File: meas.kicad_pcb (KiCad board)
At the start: 2 copper layers, 100 x 220 mm, 3 parts

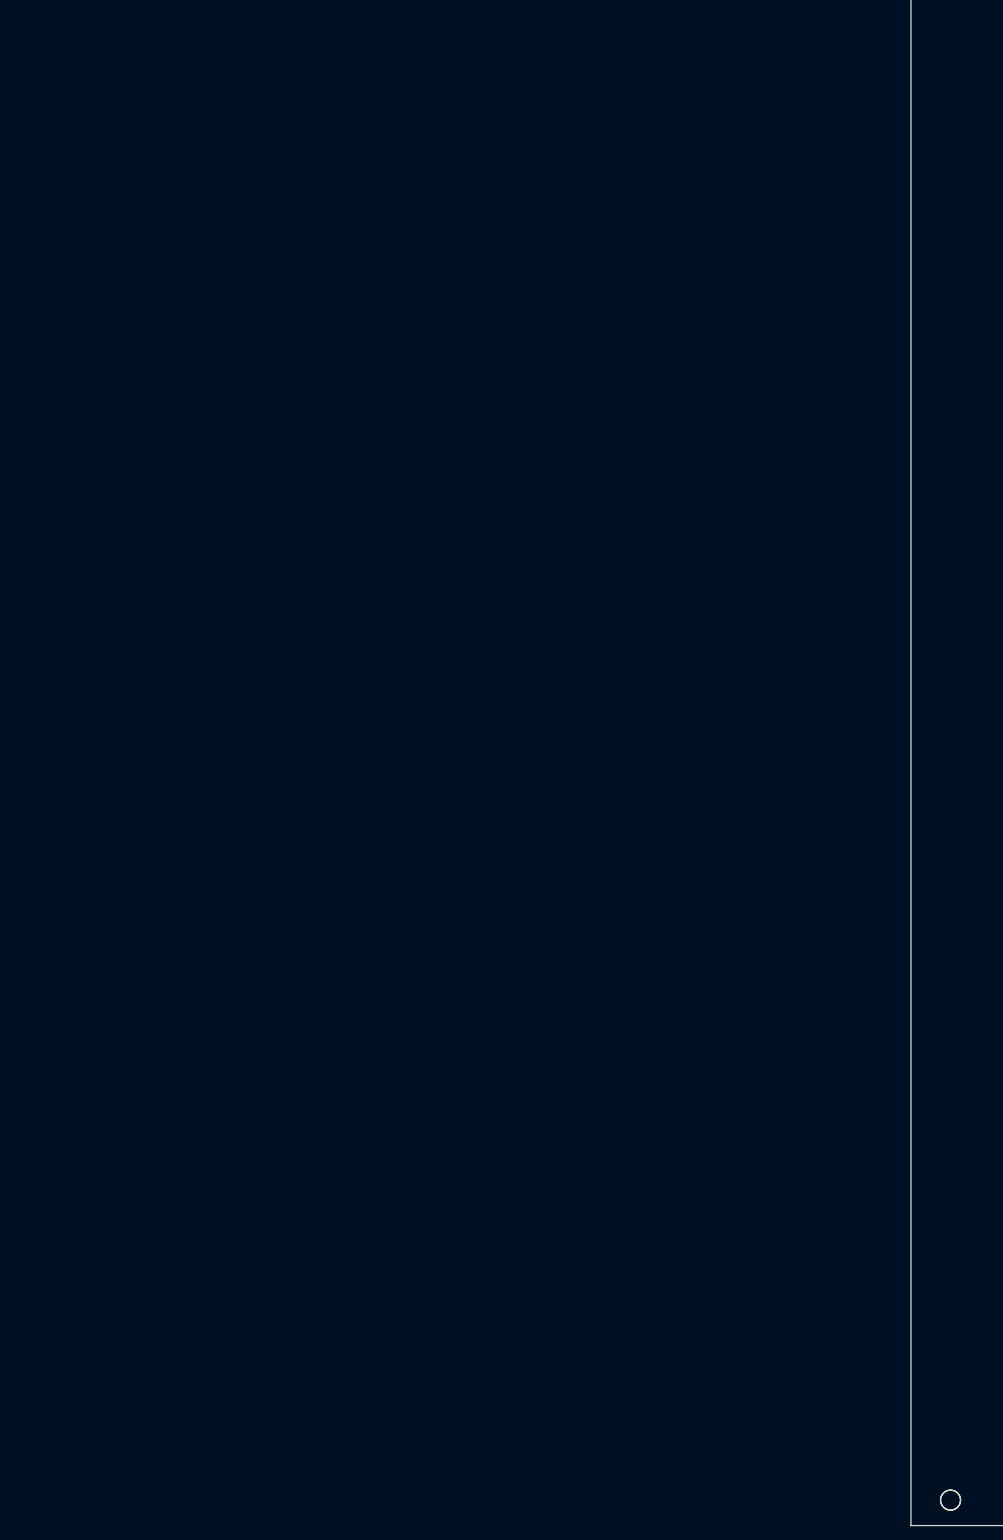
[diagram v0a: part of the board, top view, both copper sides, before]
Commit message: add export of footprint library, edit footprint links
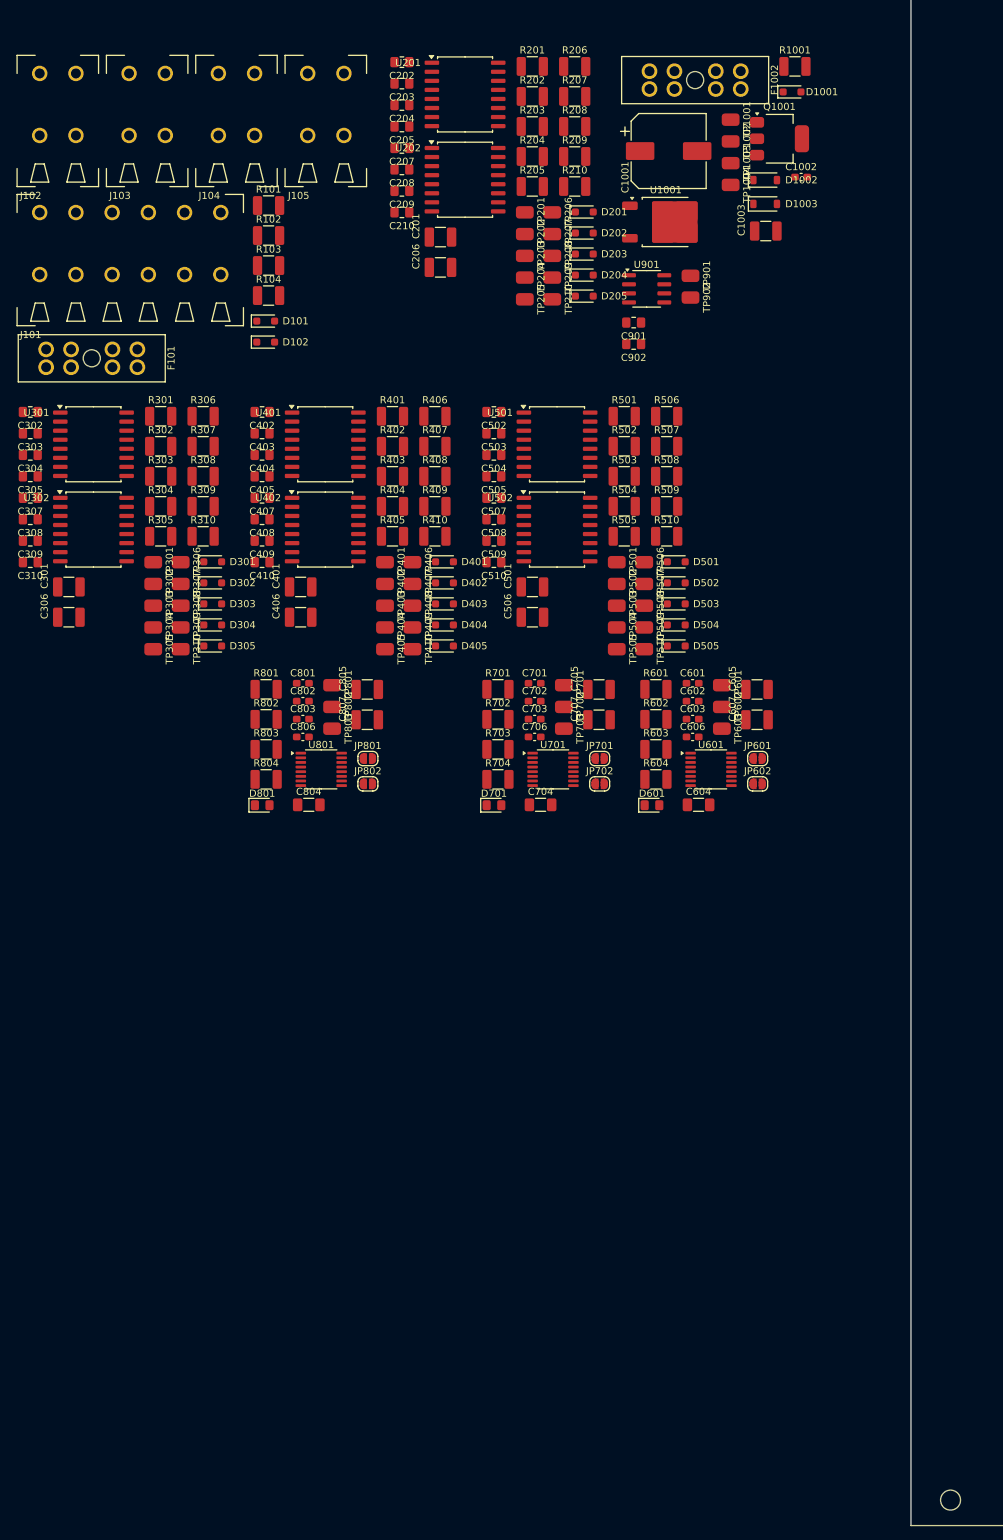
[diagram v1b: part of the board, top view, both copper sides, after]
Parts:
- removed ?: , 
- added C1001: 470u, meas:CP_Elec_10x10, F.Cu at (116.0, 67.2)
- added C1002: 1u, meas:C_0603_1608Metric_Pad1.08x0.95mm_HandSolder, F.Cu at (134.6, 70.9)
- added C1003: 10u, meas:C_1210_3225Metric_Pad1.33x2.70mm_HandSolder, F.Cu at (129.6, 78.4)
- added C201: 10u, meas:C_1210_3225Metric_Pad1.33x2.70mm_HandSolder, F.Cu at (84.0, 79.3)
- added C202: 470p, meas:C_0805_2012Metric_Pad1.18x1.45mm_HandSolder, F.Cu at (78.6, 54.7)
- added C203: 100n, meas:C_0805_2012Metric_Pad1.18x1.45mm_HandSolder, F.Cu at (78.6, 57.7)
- added C204: 100n, meas:C_0805_2012Metric_Pad1.18x1.45mm_HandSolder, F.Cu at (78.6, 60.8)
- added C205: 100n, meas:C_0805_2012Metric_Pad1.18x1.45mm_HandSolder, F.Cu at (78.6, 63.8)
- added C206: 10u, meas:C_1210_3225Metric_Pad1.33x2.70mm_HandSolder, F.Cu at (84.0, 83.5)
- added C207: 100n, meas:C_0805_2012Metric_Pad1.18x1.45mm_HandSolder, F.Cu at (78.6, 66.8)
- added C208: 470p, meas:C_0805_2012Metric_Pad1.18x1.45mm_HandSolder, F.Cu at (78.6, 69.8)
- added C209: 470p, meas:C_0805_2012Metric_Pad1.18x1.45mm_HandSolder, F.Cu at (78.6, 72.8)
- added C210: 470p, meas:C_0805_2012Metric_Pad1.18x1.45mm_HandSolder, F.Cu at (78.6, 75.8)
- added C301: 10u, meas:C_1210_3225Metric_Pad1.33x2.70mm_HandSolder, F.Cu at (31.9, 128.3)
- added C302: 470p, meas:C_0805_2012Metric_Pad1.18x1.45mm_HandSolder, F.Cu at (26.5, 103.8)
- added C303: 100n, meas:C_0805_2012Metric_Pad1.18x1.45mm_HandSolder, F.Cu at (26.5, 106.8)
- added C304: 100n, meas:C_0805_2012Metric_Pad1.18x1.45mm_HandSolder, F.Cu at (26.5, 109.8)
- added C305: 100n, meas:C_0805_2012Metric_Pad1.18x1.45mm_HandSolder, F.Cu at (26.5, 112.8)
- added C306: 10u, meas:C_1210_3225Metric_Pad1.33x2.70mm_HandSolder, F.Cu at (31.9, 132.6)
- added C307: 100n, meas:C_0805_2012Metric_Pad1.18x1.45mm_HandSolder, F.Cu at (26.5, 115.8)
- added C308: 470p, meas:C_0805_2012Metric_Pad1.18x1.45mm_HandSolder, F.Cu at (26.5, 118.9)
- added C309: 470p, meas:C_0805_2012Metric_Pad1.18x1.45mm_HandSolder, F.Cu at (26.5, 121.9)
- added C310: 470p, meas:C_0805_2012Metric_Pad1.18x1.45mm_HandSolder, F.Cu at (26.5, 124.9)
- added C401: 10u, meas:C_1210_3225Metric_Pad1.33x2.70mm_HandSolder, F.Cu at (64.4, 128.3)
- added C402: 470p, meas:C_0805_2012Metric_Pad1.18x1.45mm_HandSolder, F.Cu at (59.0, 103.8)
- added C403: 100n, meas:C_0805_2012Metric_Pad1.18x1.45mm_HandSolder, F.Cu at (59.0, 106.8)
- added C404: 100n, meas:C_0805_2012Metric_Pad1.18x1.45mm_HandSolder, F.Cu at (59.0, 109.8)
- added C405: 100n, meas:C_0805_2012Metric_Pad1.18x1.45mm_HandSolder, F.Cu at (59.0, 112.8)
- added C406: 10u, meas:C_1210_3225Metric_Pad1.33x2.70mm_HandSolder, F.Cu at (64.4, 132.6)
- added C407: 100n, meas:C_0805_2012Metric_Pad1.18x1.45mm_HandSolder, F.Cu at (59.0, 115.8)
- added C408: 470p, meas:C_0805_2012Metric_Pad1.18x1.45mm_HandSolder, F.Cu at (59.0, 118.9)
- added C409: 470p, meas:C_0805_2012Metric_Pad1.18x1.45mm_HandSolder, F.Cu at (59.0, 121.9)
- added C410: 470p, meas:C_0805_2012Metric_Pad1.18x1.45mm_HandSolder, F.Cu at (59.0, 124.9)
- added C501: 10u, meas:C_1210_3225Metric_Pad1.33x2.70mm_HandSolder, F.Cu at (96.9, 128.3)
- added C502: 470p, meas:C_0805_2012Metric_Pad1.18x1.45mm_HandSolder, F.Cu at (91.5, 103.8)
- added C503: 100n, meas:C_0805_2012Metric_Pad1.18x1.45mm_HandSolder, F.Cu at (91.5, 106.8)
- added C504: 100n, meas:C_0805_2012Metric_Pad1.18x1.45mm_HandSolder, F.Cu at (91.5, 109.8)
- added C505: 100n, meas:C_0805_2012Metric_Pad1.18x1.45mm_HandSolder, F.Cu at (91.5, 112.8)
- added C506: 10u, meas:C_1210_3225Metric_Pad1.33x2.70mm_HandSolder, F.Cu at (96.9, 132.6)
- added C507: 100n, meas:C_0805_2012Metric_Pad1.18x1.45mm_HandSolder, F.Cu at (91.5, 115.8)
- added C508: 470p, meas:C_0805_2012Metric_Pad1.18x1.45mm_HandSolder, F.Cu at (91.5, 118.9)
- added C509: 470p, meas:C_0805_2012Metric_Pad1.18x1.45mm_HandSolder, F.Cu at (91.5, 121.9)
- added C510: 470p, meas:C_0805_2012Metric_Pad1.18x1.45mm_HandSolder, F.Cu at (91.5, 124.9)
- added C601: 1u, meas:C_0603_1608Metric_Pad1.08x0.95mm_HandSolder, F.Cu at (119.4, 141.9)
- added C602: 1u, meas:C_0603_1608Metric_Pad1.08x0.95mm_HandSolder, F.Cu at (119.4, 144.4)
- added C603: 1u, meas:C_0603_1608Metric_Pad1.08x0.95mm_HandSolder, F.Cu at (119.4, 146.9)
- added C604: 47n, meas:C_1206_3216Metric_Pad1.33x1.80mm_HandSolder, F.Cu at (120.2, 158.9)
- added C605: 10u, meas:C_1210_3225Metric_Pad1.33x2.70mm_HandSolder, F.Cu at (128.4, 142.7)
- added C606: 1u, meas:C_0603_1608Metric_Pad1.08x0.95mm_HandSolder, F.Cu at (119.4, 149.4)
- added C607: 10u, meas:C_1210_3225Metric_Pad1.33x2.70mm_HandSolder, F.Cu at (128.4, 147.0)
- added C701: 1u, meas:C_0603_1608Metric_Pad1.08x0.95mm_HandSolder, F.Cu at (97.2, 141.9)
- added C702: 1u, meas:C_0603_1608Metric_Pad1.08x0.95mm_HandSolder, F.Cu at (97.2, 144.4)
- added C703: 1u, meas:C_0603_1608Metric_Pad1.08x0.95mm_HandSolder, F.Cu at (97.2, 146.9)
- added C704: 47n, meas:C_1206_3216Metric_Pad1.33x1.80mm_HandSolder, F.Cu at (98.0, 158.9)
- added C705: 10u, meas:C_1210_3225Metric_Pad1.33x2.70mm_HandSolder, F.Cu at (106.2, 142.7)
- added C706: 1u, meas:C_0603_1608Metric_Pad1.08x0.95mm_HandSolder, F.Cu at (97.2, 149.4)
- added C707: 10u, meas:C_1210_3225Metric_Pad1.33x2.70mm_HandSolder, F.Cu at (106.2, 147.0)
- added C801: 1u, meas:C_0603_1608Metric_Pad1.08x0.95mm_HandSolder, F.Cu at (64.7, 141.9)
- added C802: 1u, meas:C_0603_1608Metric_Pad1.08x0.95mm_HandSolder, F.Cu at (64.7, 144.4)
- added C803: 1u, meas:C_0603_1608Metric_Pad1.08x0.95mm_HandSolder, F.Cu at (64.7, 146.9)
- added C804: 47n, meas:C_1206_3216Metric_Pad1.33x1.80mm_HandSolder, F.Cu at (65.5, 158.9)
- added C805: 10u, meas:C_1210_3225Metric_Pad1.33x2.70mm_HandSolder, F.Cu at (73.7, 142.7)
- added C806: 1u, meas:C_0603_1608Metric_Pad1.08x0.95mm_HandSolder, F.Cu at (64.7, 149.4)
- added C807: 10u, meas:C_1210_3225Metric_Pad1.33x2.70mm_HandSolder, F.Cu at (73.7, 147.0)
- added C901: 100n, meas:C_0805_2012Metric_Pad1.18x1.45mm_HandSolder, F.Cu at (111.1, 91.3)
- added C902: 1n, meas:C_0805_2012Metric_Pad1.18x1.45mm_HandSolder, F.Cu at (111.1, 94.3)
- added D1001: D_TVS, meas:D_SOD-323_HandSoldering, F.Cu at (133.3, 58.9)
- added D1002: 1N4148, meas:D_SOD-123, F.Cu at (129.6, 71.3)
- added D1003: 1N4148, meas:D_SOD-123, F.Cu at (129.6, 74.6)
- added D101: D_TVS, meas:D_SOD-323_HandSoldering, F.Cu at (59.5, 91.1)
- added D102: D_TVS, meas:D_SOD-323_HandSoldering, F.Cu at (59.5, 94.0)
- added D201: D_TVS, meas:D_SOD-323_HandSoldering, F.Cu at (104.2, 75.8)
- added D202: D_TVS, meas:D_SOD-323_HandSoldering, F.Cu at (104.2, 78.7)
- added D203: D_TVS, meas:D_SOD-323_HandSoldering, F.Cu at (104.2, 81.7)
- added D204: D_TVS, meas:D_SOD-323_HandSoldering, F.Cu at (104.2, 84.6)
- added D205: PDZ5.6B115, meas:D_SOD-323_HandSoldering, F.Cu at (104.2, 87.6)
- added D301: D_TVS, meas:D_SOD-323_HandSoldering, F.Cu at (52.1, 124.8)
- added D302: D_TVS, meas:D_SOD-323_HandSoldering, F.Cu at (52.1, 127.8)
- added D303: D_TVS, meas:D_SOD-323_HandSoldering, F.Cu at (52.1, 130.7)
- added D304: D_TVS, meas:D_SOD-323_HandSoldering, F.Cu at (52.1, 133.7)
- added D305: PDZ5.6B115, meas:D_SOD-323_HandSoldering, F.Cu at (52.1, 136.6)
- added D401: D_TVS, meas:D_SOD-323_HandSoldering, F.Cu at (84.6, 124.8)
- added D402: D_TVS, meas:D_SOD-323_HandSoldering, F.Cu at (84.6, 127.8)
- added D403: D_TVS, meas:D_SOD-323_HandSoldering, F.Cu at (84.6, 130.7)
- added D404: D_TVS, meas:D_SOD-323_HandSoldering, F.Cu at (84.6, 133.7)
- added D405: PDZ5.6B115, meas:D_SOD-323_HandSoldering, F.Cu at (84.6, 136.6)
- added D501: D_TVS, meas:D_SOD-323_HandSoldering, F.Cu at (117.1, 124.8)
- added D502: D_TVS, meas:D_SOD-323_HandSoldering, F.Cu at (117.1, 127.8)
- added D503: D_TVS, meas:D_SOD-323_HandSoldering, F.Cu at (117.1, 130.7)
- added D504: D_TVS, meas:D_SOD-323_HandSoldering, F.Cu at (117.1, 133.7)
- added D505: PDZ5.6B115, meas:D_SOD-323_HandSoldering, F.Cu at (117.1, 136.6)
- added D601: LED, meas:LED_0805_2012Metric_Pad1.15x1.40mm_HandSolder, F.Cu at (113.7, 159.0)
- added D701: LED, meas:LED_0805_2012Metric_Pad1.15x1.40mm_HandSolder, F.Cu at (91.5, 159.0)
- added D801: LED, meas:LED_0805_2012Metric_Pad1.15x1.40mm_HandSolder, F.Cu at (59.0, 159.0)
- added F1002: Fuse_Socket, meas:FuseHolder_Blade_ATO_Littelfuse_FLR_178.6165, F.Cu at (113.3, 56.0)
- added F101: Fuse_Socket, meas:FuseHolder_Blade_ATO_Littelfuse_FLR_178.6165, F.Cu at (28.7, 95.0)
- added J101: Conn_01x06_Socket, meas:PhoenixContact_TDPT_2,5_6-SP-5,08_1x06_P5.08mm_Horizontal, F.Cu at (27.8, 75.8)
- added J102: Conn_01x02_Socket, meas:PhoenixContact_TDPT_2,5_2-SP-5,08_1x02_P5.08mm_Horizontal, F.Cu at (27.8, 56.3)
- added J103: Conn_01x02_Socket, meas:PhoenixContact_TDPT_2,5_2-SP-5,08_1x02_P5.08mm_Horizontal, F.Cu at (40.3, 56.3)
- added J104: Conn_01x02_Socket, meas:PhoenixContact_TDPT_2,5_2-SP-5,08_1x02_P5.08mm_Horizontal, F.Cu at (52.9, 56.3)
- added J105: Conn_01x02_Socket, meas:PhoenixContact_TDPT_2,5_2-SP-5,08_1x02_P5.08mm_Horizontal, F.Cu at (65.4, 56.3)
- added JP601: SolderJumper_2_Open, meas:SolderJumper-2_P1.3mm_Open_RoundedPad1.0x1.5mm, F.Cu at (128.5, 152.4)
- added JP602: SolderJumper_2_Bridged, meas:SolderJumper-2_P1.3mm_Bridged-Soldermask-Paste_RoundedPad1.0x1.5mm, F.Cu at (128.5, 156.0)
- added JP701: SolderJumper_2_Open, meas:SolderJumper-2_P1.3mm_Open_RoundedPad1.0x1.5mm, F.Cu at (106.3, 152.4)
- added JP702: SolderJumper_2_Bridged, meas:SolderJumper-2_P1.3mm_Bridged-Soldermask-Paste_RoundedPad1.0x1.5mm, F.Cu at (106.3, 156.0)
- added JP801: SolderJumper_2_Open, meas:SolderJumper-2_P1.3mm_Open_RoundedPad1.0x1.5mm, F.Cu at (73.8, 152.4)
- added JP802: SolderJumper_2_Bridged, meas:SolderJumper-2_P1.3mm_Bridged-Soldermask-Paste_RoundedPad1.0x1.5mm, F.Cu at (73.8, 156.0)
- added Q1001: DPLS350E, meas:SOT-223-3_TabPin2, F.Cu at (131.6, 65.5)
- added R1001: 5R9, meas:R_1210_3225Metric_Pad1.30x2.65mm_HandSolder, F.Cu at (133.7, 55.3)
- added R101: 0, meas:R_1210_3225Metric_Pad1.30x2.65mm_HandSolder, F.Cu at (59.9, 74.8)
- added R102: 0, meas:R_1210_3225Metric_Pad1.30x2.65mm_HandSolder, F.Cu at (59.9, 79.1)
- added R103: 100k, meas:R_1210_3225Metric_Pad1.30x2.65mm_HandSolder, F.Cu at (59.9, 83.3)
- added R104: 100k, meas:R_1210_3225Metric_Pad1.30x2.65mm_HandSolder, F.Cu at (59.9, 87.5)
- added R201: 330, meas:R_1210_3225Metric_Pad1.30x2.65mm_HandSolder, F.Cu at (96.9, 55.3)
- added R202: 1M, meas:R_1210_3225Metric_Pad1.30x2.65mm_HandSolder, F.Cu at (96.9, 59.5)
- added R203: 1M, meas:R_1210_3225Metric_Pad1.30x2.65mm_HandSolder, F.Cu at (96.9, 63.8)
- added R204: 1M, meas:R_1210_3225Metric_Pad1.30x2.65mm_HandSolder, F.Cu at (96.9, 68.0)
- added R205: 100, meas:R_1210_3225Metric_Pad1.30x2.65mm_HandSolder, F.Cu at (96.9, 72.2)
- added R206: 1M, meas:R_1210_3225Metric_Pad1.30x2.65mm_HandSolder, F.Cu at (102.8, 55.3)
- added R207: 1M, meas:R_1210_3225Metric_Pad1.30x2.65mm_HandSolder, F.Cu at (102.8, 59.5)
- added R208: 100, meas:R_1210_3225Metric_Pad1.30x2.65mm_HandSolder, F.Cu at (102.8, 63.8)
- added R209: 100, meas:R_1210_3225Metric_Pad1.30x2.65mm_HandSolder, F.Cu at (102.8, 68.0)
- added R210: 100, meas:R_1210_3225Metric_Pad1.30x2.65mm_HandSolder, F.Cu at (102.8, 72.2)
- added R301: 330, meas:R_1210_3225Metric_Pad1.30x2.65mm_HandSolder, F.Cu at (44.8, 104.4)
- added R302: 1M, meas:R_1210_3225Metric_Pad1.30x2.65mm_HandSolder, F.Cu at (44.8, 108.6)
- added R303: 1M, meas:R_1210_3225Metric_Pad1.30x2.65mm_HandSolder, F.Cu at (44.8, 112.8)
- added R304: 1M, meas:R_1210_3225Metric_Pad1.30x2.65mm_HandSolder, F.Cu at (44.8, 117.0)
- added R305: 100, meas:R_1210_3225Metric_Pad1.30x2.65mm_HandSolder, F.Cu at (44.8, 121.2)
- added R306: 1M, meas:R_1210_3225Metric_Pad1.30x2.65mm_HandSolder, F.Cu at (50.7, 104.4)
- added R307: 1M, meas:R_1210_3225Metric_Pad1.30x2.65mm_HandSolder, F.Cu at (50.7, 108.6)
- added R308: 100, meas:R_1210_3225Metric_Pad1.30x2.65mm_HandSolder, F.Cu at (50.7, 112.8)
- added R309: 100, meas:R_1210_3225Metric_Pad1.30x2.65mm_HandSolder, F.Cu at (50.7, 117.0)
- added R310: 100, meas:R_1210_3225Metric_Pad1.30x2.65mm_HandSolder, F.Cu at (50.7, 121.2)
- added R401: 330, meas:R_1210_3225Metric_Pad1.30x2.65mm_HandSolder, F.Cu at (77.3, 104.4)
- added R402: 1M, meas:R_1210_3225Metric_Pad1.30x2.65mm_HandSolder, F.Cu at (77.3, 108.6)
- added R403: 1M, meas:R_1210_3225Metric_Pad1.30x2.65mm_HandSolder, F.Cu at (77.3, 112.8)
- added R404: 1M, meas:R_1210_3225Metric_Pad1.30x2.65mm_HandSolder, F.Cu at (77.3, 117.0)
- added R405: 100, meas:R_1210_3225Metric_Pad1.30x2.65mm_HandSolder, F.Cu at (77.3, 121.2)
- added R406: 1M, meas:R_1210_3225Metric_Pad1.30x2.65mm_HandSolder, F.Cu at (83.2, 104.4)
- added R407: 1M, meas:R_1210_3225Metric_Pad1.30x2.65mm_HandSolder, F.Cu at (83.2, 108.6)
- added R408: 100, meas:R_1210_3225Metric_Pad1.30x2.65mm_HandSolder, F.Cu at (83.2, 112.8)
- added R409: 100, meas:R_1210_3225Metric_Pad1.30x2.65mm_HandSolder, F.Cu at (83.2, 117.0)
- added R410: 100, meas:R_1210_3225Metric_Pad1.30x2.65mm_HandSolder, F.Cu at (83.2, 121.2)
- added R501: 330, meas:R_1210_3225Metric_Pad1.30x2.65mm_HandSolder, F.Cu at (109.8, 104.4)
- added R502: 1M, meas:R_1210_3225Metric_Pad1.30x2.65mm_HandSolder, F.Cu at (109.8, 108.6)
- added R503: 1M, meas:R_1210_3225Metric_Pad1.30x2.65mm_HandSolder, F.Cu at (109.8, 112.8)
- added R504: 1M, meas:R_1210_3225Metric_Pad1.30x2.65mm_HandSolder, F.Cu at (109.8, 117.0)
- added R505: 100, meas:R_1210_3225Metric_Pad1.30x2.65mm_HandSolder, F.Cu at (109.8, 121.2)
- added R506: 1M, meas:R_1210_3225Metric_Pad1.30x2.65mm_HandSolder, F.Cu at (115.7, 104.4)
- added R507: 1M, meas:R_1210_3225Metric_Pad1.30x2.65mm_HandSolder, F.Cu at (115.7, 108.6)
- added R508: 100, meas:R_1210_3225Metric_Pad1.30x2.65mm_HandSolder, F.Cu at (115.7, 112.8)
- added R509: 100, meas:R_1210_3225Metric_Pad1.30x2.65mm_HandSolder, F.Cu at (115.7, 117.0)
- added R510: 100, meas:R_1210_3225Metric_Pad1.30x2.65mm_HandSolder, F.Cu at (115.7, 121.2)
- added R601: 1k, meas:R_1210_3225Metric_Pad1.30x2.65mm_HandSolder, F.Cu at (114.2, 142.7)
- added R602: 10k, meas:R_1210_3225Metric_Pad1.30x2.65mm_HandSolder, F.Cu at (114.2, 146.9)
- added R603: 100, meas:R_1210_3225Metric_Pad1.30x2.65mm_HandSolder, F.Cu at (114.2, 151.1)
- added R604: 100, meas:R_1210_3225Metric_Pad1.30x2.65mm_HandSolder, F.Cu at (114.2, 155.3)
- added R701: 1k, meas:R_1210_3225Metric_Pad1.30x2.65mm_HandSolder, F.Cu at (92.1, 142.7)
- added R702: 10k, meas:R_1210_3225Metric_Pad1.30x2.65mm_HandSolder, F.Cu at (92.1, 146.9)
- added R703: 100, meas:R_1210_3225Metric_Pad1.30x2.65mm_HandSolder, F.Cu at (92.1, 151.1)
- added R704: 100, meas:R_1210_3225Metric_Pad1.30x2.65mm_HandSolder, F.Cu at (92.1, 155.3)
- added R801: 1k, meas:R_1210_3225Metric_Pad1.30x2.65mm_HandSolder, F.Cu at (59.6, 142.7)
- added R802: 10k, meas:R_1210_3225Metric_Pad1.30x2.65mm_HandSolder, F.Cu at (59.6, 146.9)
- added R803: 100, meas:R_1210_3225Metric_Pad1.30x2.65mm_HandSolder, F.Cu at (59.6, 151.1)
- added R804: 100, meas:R_1210_3225Metric_Pad1.30x2.65mm_HandSolder, F.Cu at (59.6, 155.3)
- added TP1001: ~, meas:TP_0805_2012Metric, F.Cu at (124.7, 62.8)
- added TP1002: ~, meas:TP_0805_2012Metric, F.Cu at (124.7, 65.9)
- added TP1003: ~, meas:TP_0805_2012Metric, F.Cu at (124.7, 68.9)
- added TP1004: ~, meas:TP_0805_2012Metric, F.Cu at (124.7, 72.0)
- added TP201: ~, meas:TP_0805_2012Metric, F.Cu at (95.8, 75.8)
- added TP202: ~, meas:TP_0805_2012Metric, F.Cu at (95.8, 78.9)
- added TP203: ~, meas:TP_0805_2012Metric, F.Cu at (95.8, 81.9)
- added TP204: ~, meas:TP_0805_2012Metric, F.Cu at (95.8, 85.0)
- added TP205: ~, meas:TP_0805_2012Metric, F.Cu at (95.8, 88.0)
- added TP206: ~, meas:TP_0805_2012Metric, F.Cu at (99.7, 75.8)
- added TP207: ~, meas:TP_0805_2012Metric, F.Cu at (99.7, 78.9)
- added TP208: ~, meas:TP_0805_2012Metric, F.Cu at (99.7, 81.9)
- added TP209: ~, meas:TP_0805_2012Metric, F.Cu at (99.7, 85.0)
- added TP210: ~, meas:TP_0805_2012Metric, F.Cu at (99.7, 88.0)
- added TP301: ~, meas:TP_0805_2012Metric, F.Cu at (43.7, 124.9)
- added TP302: ~, meas:TP_0805_2012Metric, F.Cu at (43.7, 127.9)
- added TP303: ~, meas:TP_0805_2012Metric, F.Cu at (43.7, 131.0)
- added TP304: ~, meas:TP_0805_2012Metric, F.Cu at (43.7, 134.0)
- added TP305: ~, meas:TP_0805_2012Metric, F.Cu at (43.7, 137.1)
- added TP306: ~, meas:TP_0805_2012Metric, F.Cu at (47.6, 124.9)
- added TP307: ~, meas:TP_0805_2012Metric, F.Cu at (47.6, 127.9)
- added TP308: ~, meas:TP_0805_2012Metric, F.Cu at (47.6, 131.0)
- added TP309: ~, meas:TP_0805_2012Metric, F.Cu at (47.6, 134.0)
- added TP310: ~, meas:TP_0805_2012Metric, F.Cu at (47.6, 137.1)
- added TP401: ~, meas:TP_0805_2012Metric, F.Cu at (76.2, 124.9)
- added TP402: ~, meas:TP_0805_2012Metric, F.Cu at (76.2, 127.9)
- added TP403: ~, meas:TP_0805_2012Metric, F.Cu at (76.2, 131.0)
- added TP404: ~, meas:TP_0805_2012Metric, F.Cu at (76.2, 134.0)
- added TP405: ~, meas:TP_0805_2012Metric, F.Cu at (76.2, 137.1)
- added TP406: ~, meas:TP_0805_2012Metric, F.Cu at (80.1, 124.9)
- added TP407: ~, meas:TP_0805_2012Metric, F.Cu at (80.1, 127.9)
- added TP408: ~, meas:TP_0805_2012Metric, F.Cu at (80.1, 131.0)
- added TP409: ~, meas:TP_0805_2012Metric, F.Cu at (80.1, 134.0)
- added TP410: ~, meas:TP_0805_2012Metric, F.Cu at (80.1, 137.1)
- added TP501: ~, meas:TP_0805_2012Metric, F.Cu at (108.7, 124.9)
- added TP502: ~, meas:TP_0805_2012Metric, F.Cu at (108.7, 127.9)
- added TP503: ~, meas:TP_0805_2012Metric, F.Cu at (108.7, 131.0)
- added TP504: ~, meas:TP_0805_2012Metric, F.Cu at (108.7, 134.0)
- added TP505: ~, meas:TP_0805_2012Metric, F.Cu at (108.7, 137.1)
- added TP506: ~, meas:TP_0805_2012Metric, F.Cu at (112.6, 124.9)
- added TP507: ~, meas:TP_0805_2012Metric, F.Cu at (112.6, 127.9)
- added TP508: ~, meas:TP_0805_2012Metric, F.Cu at (112.6, 131.0)
- added TP509: ~, meas:TP_0805_2012Metric, F.Cu at (112.6, 134.0)
- added TP510: ~, meas:TP_0805_2012Metric, F.Cu at (112.6, 137.1)
- added TP601: ~, meas:TP_0805_2012Metric, F.Cu at (123.5, 142.1)
- added TP602: ~, meas:TP_0805_2012Metric, F.Cu at (123.5, 145.2)
- added TP603: ~, meas:TP_0805_2012Metric, F.Cu at (123.5, 148.2)
- added TP701: ~, meas:TP_0805_2012Metric, F.Cu at (101.3, 142.1)
- added TP702: ~, meas:TP_0805_2012Metric, F.Cu at (101.3, 145.2)
- added TP703: ~, meas:TP_0805_2012Metric, F.Cu at (101.3, 148.2)
- added TP801: ~, meas:TP_0805_2012Metric, F.Cu at (68.8, 142.1)
- added TP802: ~, meas:TP_0805_2012Metric, F.Cu at (68.8, 145.2)
- added TP803: ~, meas:TP_0805_2012Metric, F.Cu at (68.8, 148.2)
- added TP901: ~, meas:TP_0805_2012Metric, F.Cu at (119.1, 84.7)
- added TP902: ~, meas:TP_0805_2012Metric, F.Cu at (119.1, 87.8)
- added U1001: MC7805, meas:TO-252-2, F.Cu at (115.6, 77.2)
- added U201: Si8641BD-B-IS2, meas:SOIC-16W_7.5x10.3mm_P1.27mm, F.Cu at (87.5, 59.3)
- added U202: R05C05TE05S, meas:SOIC-16W_7.5x10.3mm_P1.27mm, F.Cu at (87.5, 71.2)
- added U301: Si8641BD-B-IS2, meas:SOIC-16W_7.5x10.3mm_P1.27mm, F.Cu at (35.3, 108.3)
- added U302: R05C05TE05S, meas:SOIC-16W_7.5x10.3mm_P1.27mm, F.Cu at (35.3, 120.3)
- added U401: Si8641BD-B-IS2, meas:SOIC-16W_7.5x10.3mm_P1.27mm, F.Cu at (67.8, 108.3)
- added U402: R05C05TE05S, meas:SOIC-16W_7.5x10.3mm_P1.27mm, F.Cu at (67.8, 120.3)
- added U501: Si8641BD-B-IS2, meas:SOIC-16W_7.5x10.3mm_P1.27mm, F.Cu at (100.4, 108.3)
- added U502: R05C05TE05S, meas:SOIC-16W_7.5x10.3mm_P1.27mm, F.Cu at (100.4, 120.3)
- added U601: ADS8665IPWR, meas:TSSOP-16_4.4x5mm_P0.65mm, F.Cu at (122.0, 153.9)
- added U701: ADS8665IPWR, meas:TSSOP-16_4.4x5mm_P0.65mm, F.Cu at (99.8, 153.9)
- added U801: ADS8665IPWR, meas:TSSOP-16_4.4x5mm_P0.65mm, F.Cu at (67.3, 153.9)
- added U901: ACS730xLCTR-20AB, meas:SOIC-8_3.9x4.9mm_P1.27mm, F.Cu at (112.9, 86.5)

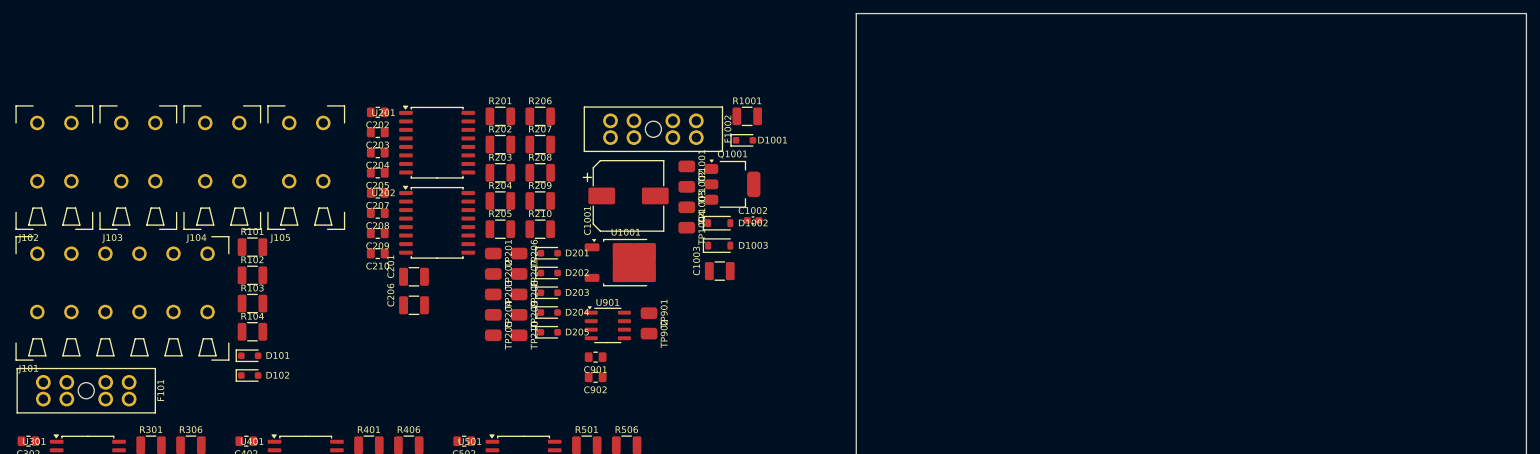
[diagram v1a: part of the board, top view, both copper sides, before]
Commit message: add connector placement
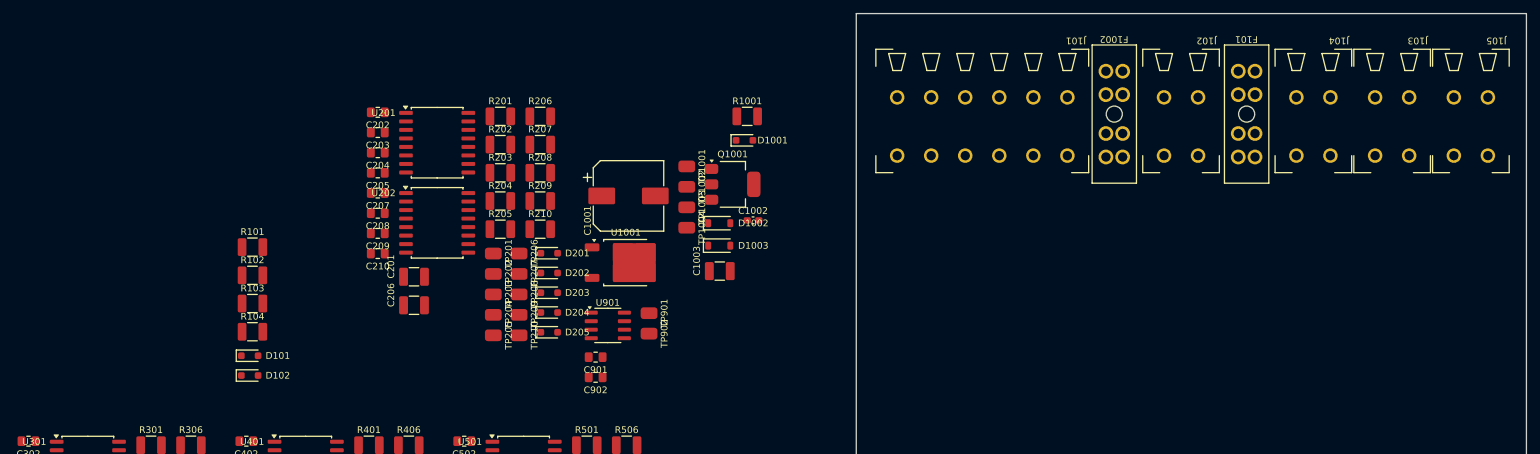
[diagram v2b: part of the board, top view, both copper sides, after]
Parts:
- moved J103 192.2 mm to (232.5, 61.2), turned to 180 degrees
- moved F101 181.4 mm to (207.0, 61.4), turned to 90 degrees
- moved J105 178.9 mm to (244.2, 61.2), turned to 180 degrees
- moved J102 173.3 mm to (201.0, 61.2), turned to 180 degrees
- moved J104 168.0 mm to (220.8, 61.2), turned to 180 degrees
- moved J101 154.4 mm to (181.5, 61.2), turned to 180 degrees
- moved F1002 74.1 mm to (187.2, 61.4), turned to 90 degrees

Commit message: add coarse placement of sub circuits
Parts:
- C901, C902, U901: moved to B.Cu
- moved C501 222.8 mm to (-106.0, 36.4)
- moved C502 222.8 mm to (-111.4, 11.8)
- moved C503 222.8 mm to (-111.4, 14.8)
- moved C504 222.8 mm to (-111.4, 17.8)
- moved C505 222.8 mm to (-111.4, 20.9)
- moved C506 222.8 mm to (-106.0, 40.6)
- moved C507 222.8 mm to (-111.4, 23.9)
- moved C508 222.8 mm to (-111.4, 26.9)
- moved C509 222.8 mm to (-111.4, 29.9)
- moved C510 222.8 mm to (-111.4, 32.9)
- moved D501 222.8 mm to (-85.8, 32.8)
- moved D502 222.8 mm to (-85.8, 35.8)
- moved D503 222.8 mm to (-85.8, 38.7)
- moved D504 222.8 mm to (-85.8, 41.7)
- moved D505 222.8 mm to (-85.8, 44.6)
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
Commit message: add adc sub-layout
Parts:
- moved TP803 292.0 mm to (240.0, 88.2)
- moved R703 272.4 mm to (235.3, 153.1)
- moved R603 270.2 mm to (235.3, 127.7)
- moved R803 268.7 mm to (235.3, 178.5)
- moved R704 266.0 mm to (229.8, 151.5), turned to 180 degrees
- moved TP702 265.7 mm to (234.3, 162.7), turned to 180 degrees
- moved R604 265.6 mm to (229.8, 126.1), turned to 180 degrees
- moved C703 265.4 mm to (231.0, 160.0), turned to 180 degrees
- moved R804 264.4 mm to (229.8, 176.9), turned to 180 degrees
- moved C706 264.3 mm to (231.0, 157.4), turned to 180 degrees
- moved D701 263.7 mm to (225.4, 163.7), turned to 180 degrees
- moved C705 261.8 mm to (235.3, 159.9), turned to 180 degrees
- moved C702 261.3 mm to (225.7, 162.0), turned to 180 degrees
- moved R702 261.2 mm to (220.8, 163.0)
- moved R701 261.0 mm to (222.4, 151.5), turned to 180 degrees
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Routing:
- net /GND_ISO_T: track 0.00 -> 43.0 mm, vias 0 -> 2
- net /GND_ISO_I: track 0.00 -> 43.0 mm, vias 0 -> 2
- net /GND_ISO_U: track 0.00 -> 43.0 mm, vias 0 -> 2
- net /+5VA_ISO_U: track 0.00 -> 23.7 mm, vias 0 -> 2
- net /+5VA_ISO_I: track 0.00 -> 23.7 mm, vias 0 -> 2
- net /+5VA_ISO_T: track 0.00 -> 23.7 mm, vias 0 -> 2
- net Net-(U601-REFIO): track 0.00 -> 10.2 mm
- net Net-(U701-REFIO): track 0.00 -> 10.2 mm
- net Net-(U801-REFIO): track 0.00 -> 10.2 mm
- net Net-(JP701-B): track 0.00 -> 8.57 mm
- net Net-(JP601-B): track 0.00 -> 8.57 mm
- net Net-(JP801-B): track 0.00 -> 8.57 mm
- net Net-(U701-AIN_P): track 0.00 -> 7.79 mm
- net Net-(U601-AIN_P): track 0.00 -> 7.79 mm
- net Net-(U801-AIN_P): track 0.00 -> 7.79 mm
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- added copper zone on F.Cu, net /GND_ISO_I
- added copper zone on F.Cu, net /GND_ISO_T
- added copper zone on F.Cu, net /GND_ISO_U
